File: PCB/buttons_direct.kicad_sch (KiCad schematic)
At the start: 11 parts

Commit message: task: write matched LCSC part numbers into the schematic
Adds scripts/apply_lcsc_fields.py, which clones each symbol's existing
Manufacturer_Part_Number property (same indentation/effects) into a new
'LCSC' field with the matched code -- the field name the Fabrication
Toolkit plugin already installed in this repo recognizes for JLCPCB BOM
matching.

Applied the 31 confirmed matches from jlc_match.py across all sheets
(68 individual references). C_BUCK_OUT1 and R_ISET1 are left without an
LCSC field -- JLC doesn't stock those exact Yageo part numbers, to be
sorted out separately.

Verified: kicad-cli sch export bom round-trips every LCSC value
correctly, and ERC reports 0 violations.

Also switched jlc_match.py's BOM export to unranged references so each
match maps cleanly to individual schematic symbols.

Co-Authored-By: Claude Sonnet 5 <noreply@anthropic.com>
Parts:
- SW_MACRO1, SW_MACRO2, SW_MACRO3, SW_MACRO4, SW_MACRO5, SW_MACRO6: LCSC (none) -> C319409
- SW_THR_DN1, SW_THR_UP1, SW_TRIG_DIG1, SW_VOL_DN1, SW_VOL_UP1: LCSC (none) -> C110293
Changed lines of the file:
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@@
+			)
+		)
+		(property "LCSC" "C319409"
+			(at 0 0 0)
+			(hide yes)
+			(show_name no)
+			(do_not_autoplace no)
+			(effects
+				(font
+					(size 1.27 1.27)
+				)
 			)
 		)
@@
 			)
 		)
+		(property "LCSC" "C319409"
+			(at 0 0 0)
+			(hide yes)
+			(show_name no)
+			(do_not_autoplace no)
+			(effects
+				(font
+					(size 1.27 1.27)
+				)
+			)
+		)
 		(pin "1"
 		)
@@
 			)
 		)
+		(property "LCSC" "C319409"
+			(at 0 0 0)
+			(hide yes)
+			(show_name no)
+			(do_not_autoplace no)
+			(effects
+				(font
+					(size 1.27 1.27)
+				)
+			)
+		)
 		(pin "1"
 		)
@@
 			)
 		)
+		(property "LCSC" "C110293"
+			(at 0 0 0)
+			(hide yes)
+			(show_name no)
+			(do_not_autoplace no)
+			(effects
+				(font
+					(size 1.27 1.27)
+				)
+			)
+		)
 		(pin "1"
 		)
@@
 			)
 		)
+		(property "LCSC" "C110293"
+			(at 0 0 0)
+			(hide yes)
+			(show_name no)
+			(do_not_autoplace no)
+			(effects
+				(font
+					(size 1.27 1.27)
+				)
+			)
+		)
 		(pin "1"
 		)
@@
 			)
 		)
+		(property "LCSC" "C319409"
+			(at 0 0 0)
+			(hide yes)
+			(show_name no)
+			(do_not_autoplace no)
+			(effects
+				(font
+					(size 1.27 1.27)
+				)
+			)
+		)
 		(pin "1"
 		)
@@
 			)
 		)
+		(property "LCSC" "C110293"
+			(at 0 0 0)
+			(hide yes)
+			(show_name no)
+			(do_not_autoplace no)
+			(effects
+				(font
+					(size 1.27 1.27)
+				)
+			)
+		)
 		(pin "1"
 		)
@@
 			)
 		)
+		(property "LCSC" "C319409"
+			(at 0 0 0)
+			(hide yes)
+			(show_name no)
+			(do_not_autoplace no)
+			(effects
+				(font
+					(size 1.27 1.27)
+				)
+			)
+		)
 		(pin "1"
 		)
@@
 			)
 		)
+		(property "LCSC" "C110293"
+			(at 0 0 0)
+			(hide yes)
+			(show_name no)
+			(do_not_autoplace no)
+			(effects
+				(font
+					(size 1.27 1.27)
+				)
+			)
+		)
 		(pin "1"
 		)
@@
 			)
 		)
+		(property "LCSC" "C110293"
+			(at 0 0 0)
+			(hide yes)
+			(show_name no)
+			(do_not_autoplace no)
+			(effects
+				(font
+					(size 1.27 1.27)
+				)
+			)
+		)
 		(pin "1"
 		)
@@
 			(at 0 0 0)
 			(hide yes)
+			(show_name no)
+			(do_not_autoplace no)
+			(effects
+				(font
+					(size 1.27 1.27)
+				)
+			)
+		)
+		(property "LCSC" "C319409"
+			(at 0 0 0)
+			(hide yes)

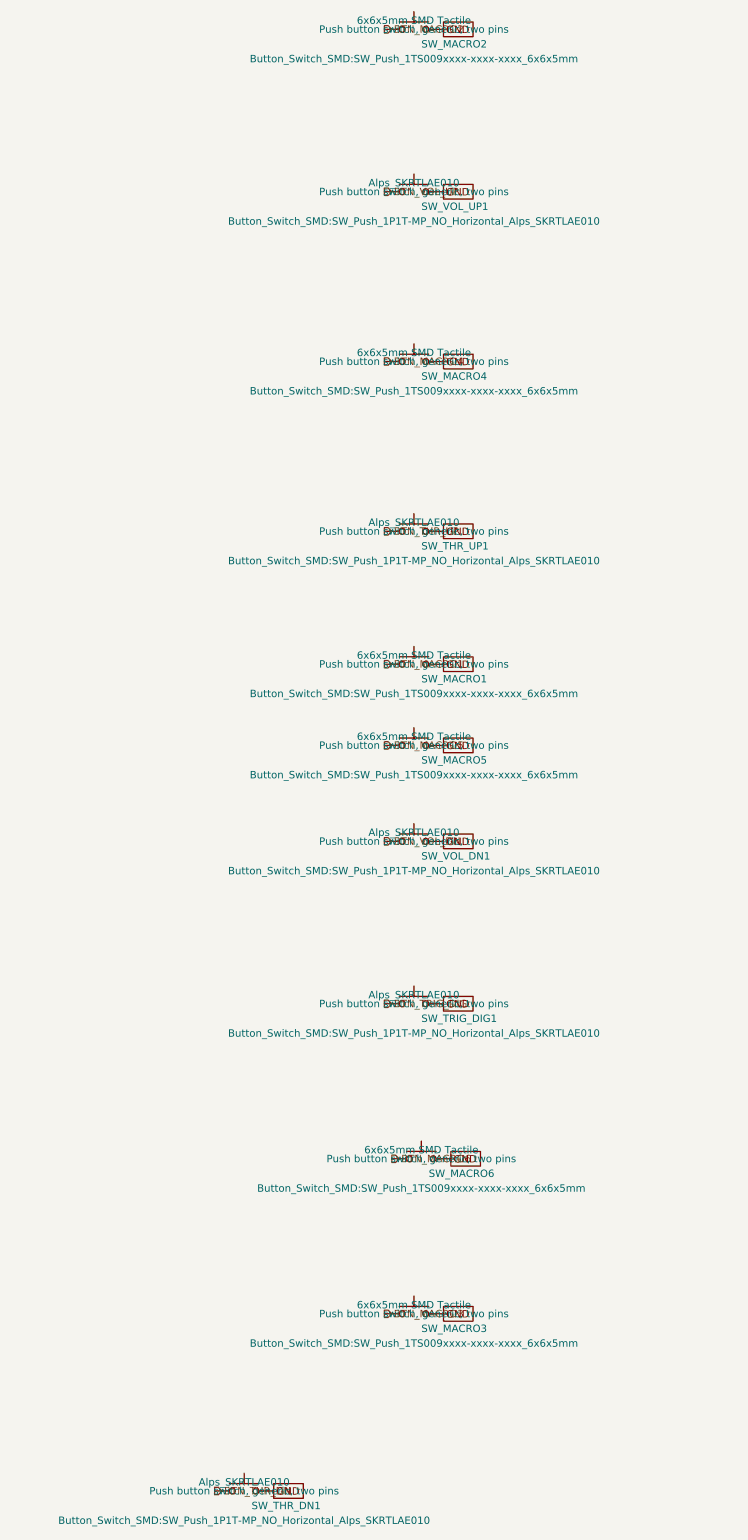
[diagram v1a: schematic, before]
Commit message: fix: make every BOM Value unambiguous for the fab, and switch D_INV_ISO1 to SOT-323 (#61)
* fix: make every BOM Value unambiguous for the fab, and switch D_INV_ISO1 to SOT-323

PCBWay flagged D_INV_ISO1: "BAT54W" is SOT-323 from nearly every maker, but we
had picked Yangjie's SOD-123 variant. A fab only sees Designator, Footprint,
Quantity and Value in the BOM (never MF/MPN/LCSC), so a bare part name is
ambiguous. Fixes the class of problem, not just this part:

- Every component's Value is now "<label> | <MPN> | <manufacturer> | <package>"
  (label dropped when it repeats the MPN; commas/periods stripped so the CSV
  never needs quoting). BT1 keeps its RIGHT-ANGLE HORIZONTAL note. Applied to
  all 81 parts across every sheet and the PCB.
- scripts/bom_values.py builds, applies, and checks these values, including
  that the PCB copy of Value/MF/MPN/footprint matches the schematic. New
  footprints must be added to its package table on purpose; hand-sourced parts
  with no MPN (J_STICK1) are listed explicitly.
- D_INV_ISO1 -> Diodes BAT54W-7-F in SOT-323 (common part, several makers).
  Pin 1 anode / pin 2 not connected / pin 3 cathode, confirmed against
  Nexperia's numbered pinning table and Diodes' datasheet. Uses KiCad's
  Diode:BAT54W symbol; PCB footprint replaced and rerouted. Electrically the
  same BAT54 family (30V, 200mA, 2uA leakage at 25V), so the SPICE model and
  scripts/spice/latch_sim.py still pass.
- Layout diagrams now say AO3401A for Q_PWR1 (they were stale since it was
  swapped from DMG2305UX) and BAT54W-7-F/SOT-323 for D_INV_ISO1.
- Repo CLAUDE.md documents the Value rule and the script.

ERC/DRC clean; production files regenerated.

Co-Authored-By: Claude Sonnet 5 <noreply@anthropic.com>

* chore: commit KiCad project settings (reordered used-designators list)

Co-Authored-By: Claude Sonnet 5 <noreply@anthropic.com>

---------

Co-authored-by: Claude Sonnet 5 <noreply@anthropic.com>
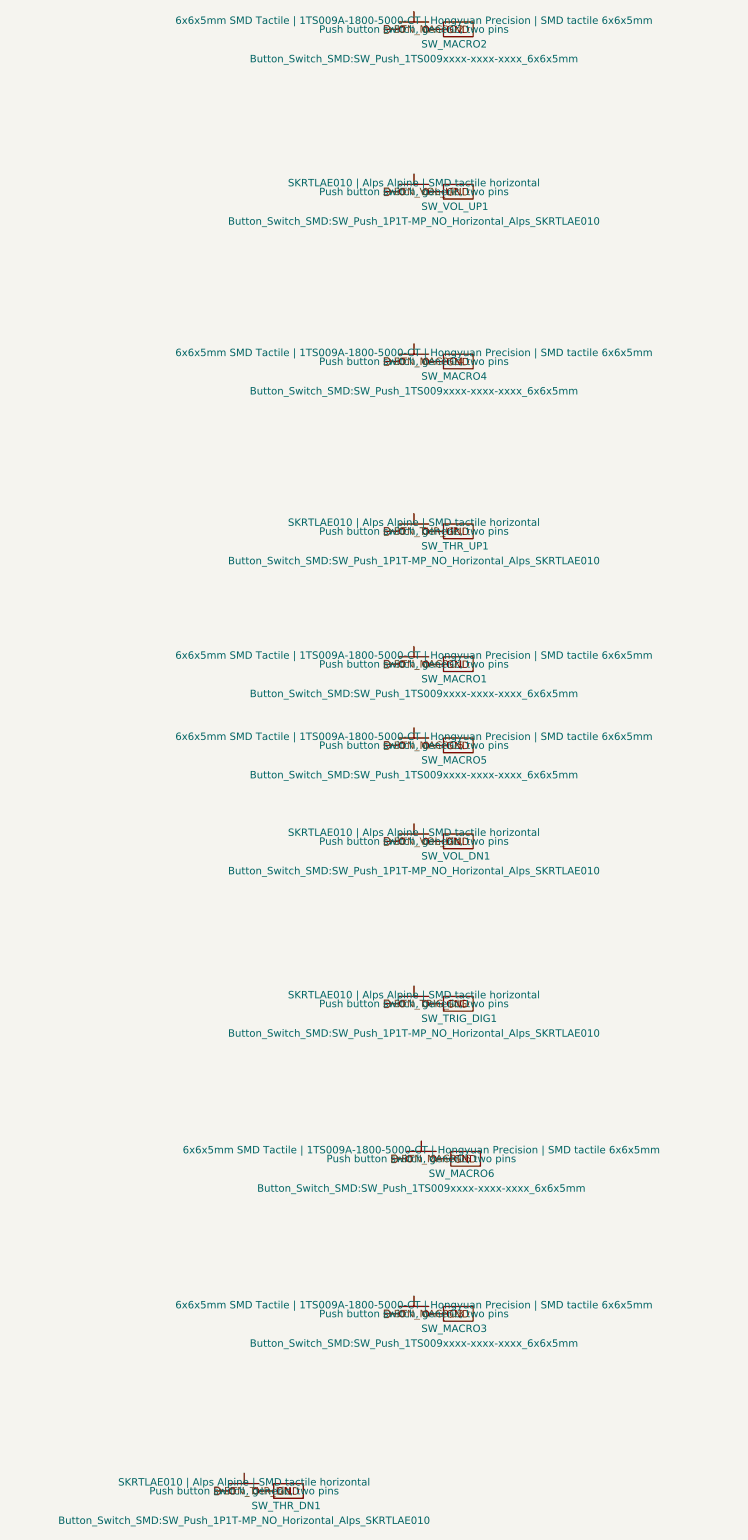
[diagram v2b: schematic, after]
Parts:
- SW_MACRO1, SW_MACRO2, SW_MACRO3, SW_MACRO4, SW_MACRO5, SW_MACRO6: value 6x6x5mm SMD Tactile -> 6x6x5mm SMD Tactile | 1TS009A-1800-5000-CT | Hongyuan Precision | SMD tactile 6x6x5mm
- SW_THR_DN1, SW_THR_UP1, SW_TRIG_DIG1, SW_VOL_DN1, SW_VOL_UP1: value Alps_SKRTLAE010 -> SKRTLAE010 | Alps Alpine | SMD tactile horizontal
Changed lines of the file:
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@@
 			)
 		)
-		(property "Value" "6x6x5mm SMD Tactile"
+		(property "Value" "6x6x5mm SMD Tactile | 1TS009A-1800-5000-CT | Hongyuan Precision | SMD tactile 6x6x5mm"
 			(at 162.56 87.376 0)
 			(show_name no)
@@
 			)
 		)
-		(property "Value" "6x6x5mm SMD Tactile"
+		(property "Value" "6x6x5mm SMD Tactile | 1TS009A-1800-5000-CT | Hongyuan Precision | SMD tactile 6x6x5mm"
 			(at 162.56 -21.844 0)
 			(show_name no)
@@
 			)
 		)
-		(property "Value" "6x6x5mm SMD Tactile"
+		(property "Value" "6x6x5mm SMD Tactile | 1TS009A-1800-5000-CT | Hongyuan Precision | SMD tactile 6x6x5mm"
 			(at 162.56 101.346 0)
 			(show_name no)
@@
 			)
 		)
-		(property "Value" "Alps_SKRTLAE010"
+		(property "Value" "SKRTLAE010 | Alps Alpine | SMD tactile horizontal"
 			(at 162.56 145.796 0)
 			(show_name no)
@@
 			)
 		)
-		(property "Value" "Alps_SKRTLAE010"
+		(property "Value" "SKRTLAE010 | Alps Alpine | SMD tactile horizontal"
 			(at 162.56 117.856 0)
 			(show_name no)
@@
 			)
 		)
-		(property "Value" "6x6x5mm SMD Tactile"
+		(property "Value" "6x6x5mm SMD Tactile | 1TS009A-1800-5000-CT | Hongyuan Precision | SMD tactile 6x6x5mm"
 			(at 162.56 199.136 0)
 			(show_name no)
@@
 			)
 		)
-		(property "Value" "Alps_SKRTLAE010"
+		(property "Value" "SKRTLAE010 | Alps Alpine | SMD tactile horizontal"
 			(at 162.56 64.516 0)
 			(show_name no)
@@
 			)
 		)
-		(property "Value" "6x6x5mm SMD Tactile"
+		(property "Value" "6x6x5mm SMD Tactile | 1TS009A-1800-5000-CT | Hongyuan Precision | SMD tactile 6x6x5mm"
 			(at 162.56 35.306 0)
 			(show_name no)
@@
 			)
 		)
-		(property "Value" "Alps_SKRTLAE010"
+		(property "Value" "SKRTLAE010 | Alps Alpine | SMD tactile horizontal"
 			(at 162.56 6.096 0)
 			(show_name no)
@@
 			)
 		)
-		(property "Value" "Alps_SKRTLAE010"
+		(property "Value" "SKRTLAE010 | Alps Alpine | SMD tactile horizontal"
 			(at 133.35 229.616 0)
 			(show_name no)
@@
 			)
 		)
-		(property "Value" "6x6x5mm SMD Tactile"
+		(property "Value" "6x6x5mm SMD Tactile | 1TS009A-1800-5000-CT | Hongyuan Precision | SMD tactile 6x6x5mm"
 			(at 163.83 172.466 0)
 			(show_name no)
